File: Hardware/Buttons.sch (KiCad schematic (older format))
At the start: 12 parts, among them SW2 SW_Push, SW3 SW_Push, SW4 SW_Push

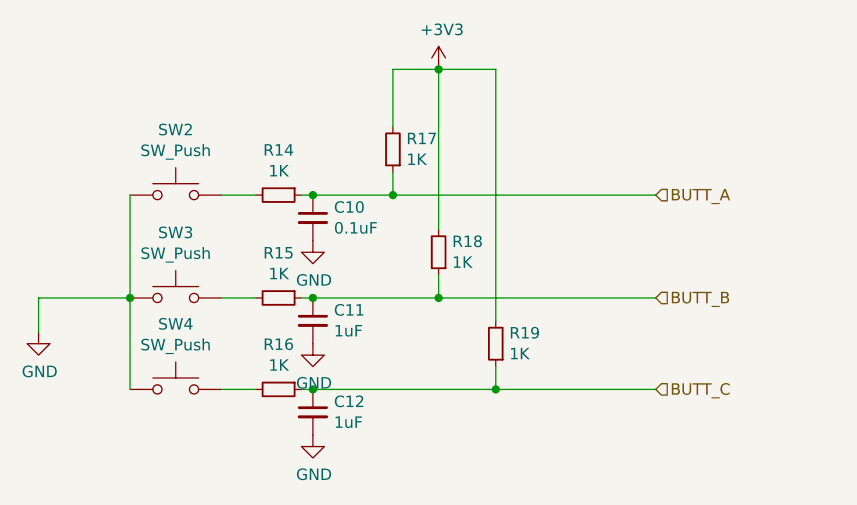
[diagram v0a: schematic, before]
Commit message: Added ADC instead of opamp. Added stiching
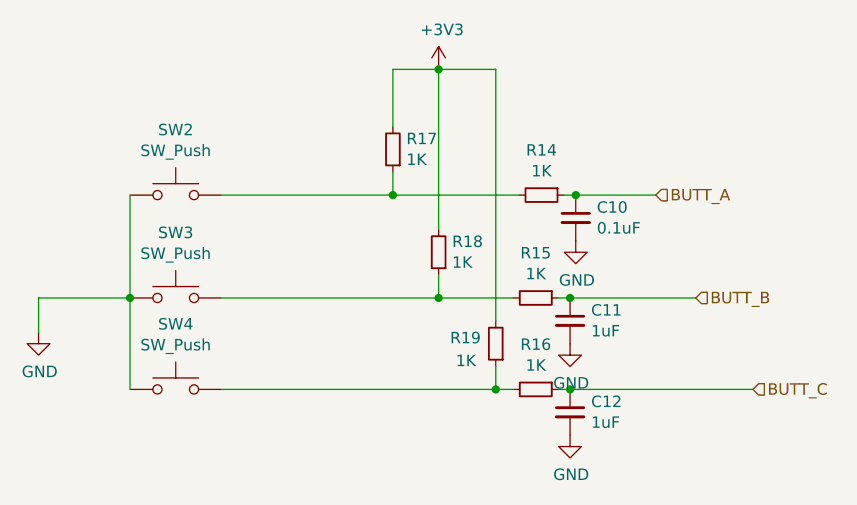
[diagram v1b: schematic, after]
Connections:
- net BUTT_A: no longer R17.1
- net BUTT_B: no longer R18.1
- net BUTT_C: no longer R19.1
- net at R14.2, SW2.2: now also R17.1
- net at R15.2, SW3.2: now also R18.1
- net at R16.2, SW4.2: now also R19.1
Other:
- moved on the sheet: C10, C11, C12, R14, R15, R16
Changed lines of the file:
@@
 L Device:R_Small R14
 U 1 1 5F81D440
-P 5450 2800
-F 0 "R14" V 5254 2800 50  0000 C CNN
-F 1 "1K" V 5345 2800 50  0000 C CNN
-F 2 "Resistor_SMD:R_0603_1608Metric_Pad1.05x0.95mm_HandSolder" H 5450 2800 50  0001 C CNN
-F 3 "~" H 5450 2800 50  0001 C CNN
-	1    5450 2800
+P 6600 2800
+F 0 "R14" V 6404 2800 50  0000 C CNN
+F 1 "1K" V 6495 2800 50  0000 C CNN
+F 2 "Resistor_SMD:R_0603_1608Metric_Pad1.05x0.95mm_HandSolder" H 6600 2800 50  0001 C CNN
+F 3 "~" H 6600 2800 50  0001 C CNN
+	1    6600 2800
 	0    1    1    0
 $EndComp
@@
 L Device:R_Small R15
 U 1 1 5F81DD10
-P 5450 3250
-F 0 "R15" V 5254 3250 50  0000 C CNN
-F 1 "1K" V 5345 3250 50  0000 C CNN
-F 2 "Resistor_SMD:R_0603_1608Metric_Pad1.05x0.95mm_HandSolder" H 5450 3250 50  0001 C CNN
-F 3 "~" H 5450 3250 50  0001 C CNN
-	1    5450 3250
+P 6575 3250
+F 0 "R15" V 6379 3250 50  0000 C CNN
+F 1 "1K" V 6470 3250 50  0000 C CNN
+F 2 "Resistor_SMD:R_0603_1608Metric_Pad1.05x0.95mm_HandSolder" H 6575 3250 50  0001 C CNN
+F 3 "~" H 6575 3250 50  0001 C CNN
+	1    6575 3250
 	0    1    1    0
 $EndComp
@@
 L Device:R_Small R16
 U 1 1 5F81E057
-P 5450 3650
-F 0 "R16" V 5254 3650 50  0000 C CNN
-F 1 "1K" V 5345 3650 50  0000 C CNN
-F 2 "Resistor_SMD:R_0603_1608Metric_Pad1.05x0.95mm_HandSolder" H 5450 3650 50  0001 C CNN
-F 3 "~" H 5450 3650 50  0001 C CNN
-	1    5450 3650
+P 6575 3650
+F 0 "R16" V 6379 3650 50  0000 C CNN
+F 1 "1K" V 6470 3650 50  0000 C CNN
+F 2 "Resistor_SMD:R_0603_1608Metric_Pad1.05x0.95mm_HandSolder" H 6575 3650 50  0001 C CNN
+F 3 "~" H 6575 3650 50  0001 C CNN
+	1    6575 3650
 	0    1    1    0
 $EndComp
@@
 L Device:C_Small C10
 U 1 1 5F81E4AB
-P 5600 2900
-F 0 "C10" H 5692 2946 50  0000 L CNN
-F 1 "0.1uF" H 5692 2855 50  0000 L CNN
-F 2 "Capacitor_SMD:C_0603_1608Metric_Pad1.05x0.95mm_HandSolder" H 5600 2900 50  0001 C CNN
-F 3 "~" H 5600 2900 50  0001 C CNN
-	1    5600 2900
+P 6750 2900
+F 0 "C10" H 6842 2946 50  0000 L CNN
+F 1 "0.1uF" H 6842 2855 50  0000 L CNN
+F 2 "Capacitor_SMD:C_0603_1608Metric_Pad1.05x0.95mm_HandSolder" H 6750 2900 50  0001 C CNN
+F 3 "~" H 6750 2900 50  0001 C CNN
+	1    6750 2900
 	1    0    0    -1
 $EndComp
@@
 L Device:C_Small C11
 U 1 1 5F81ED16
-P 5600 3350
-F 0 "C11" H 5692 3396 50  0000 L CNN
-F 1 "1uF" H 5692 3305 50  0000 L CNN
-F 2 "Capacitor_SMD:C_0603_1608Metric_Pad1.05x0.95mm_HandSolder" H 5600 3350 50  0001 C CNN
-F 3 "~" H 5600 3350 50  0001 C CNN
-	1    5600 3350
+P 6725 3350
+F 0 "C11" H 6817 3396 50  0000 L CNN
+F 1 "1uF" H 6817 3305 50  0000 L CNN
+F 2 "Capacitor_SMD:C_0603_1608Metric_Pad1.05x0.95mm_HandSolder" H 6725 3350 50  0001 C CNN
+F 3 "~" H 6725 3350 50  0001 C CNN
+	1    6725 3350
 	1    0    0    -1
 $EndComp
@@
 L Device:C_Small C12
 U 1 1 5F81F0E5
-P 5600 3750
-F 0 "C12" H 5692 3796 50  0000 L CNN
-F 1 "1uF" H 5692 3705 50  0000 L CNN
-F 2 "Capacitor_SMD:C_0603_1608Metric_Pad1.05x0.95mm_HandSolder" H 5600 3750 50  0001 C CNN
-F 3 "~" H 5600 3750 50  0001 C CNN
-	1    5600 3750
+P 6725 3750
+F 0 "C12" H 6817 3796 50  0000 L CNN
+F 1 "1uF" H 6817 3705 50  0000 L CNN
+F 2 "Capacitor_SMD:C_0603_1608Metric_Pad1.05x0.95mm_HandSolder" H 6725 3750 50  0001 C CNN
+F 3 "~" H 6725 3750 50  0001 C CNN
+	1    6725 3750
 	1    0    0    -1
 $EndComp
-Wire Wire Line
-	5200 2800 5350 2800
-Wire Wire Line
-	5200 3250 5350 3250
-Wire Wire Line
-	5200 3650 5350 3650
 $Comp
 L power:GND #PWR0129
 U 1 1 5F81F72F
-P 5600 3000
-F 0 "#PWR0129" H 5600 2750 50  0001 C CNN
-F 1 "GND" H 5605 2827 50  0000 C CNN
-F 2 "" H 5600 3000 50  0001 C CNN
-F 3 "" H 5600 3000 50  0001 C CNN
-	1    5600 3000
+P 6750 3000
+F 0 "#PWR0129" H 6750 2750 50  0001 C CNN
+F 1 "GND" H 6755 2827 50  0000 C CNN
+F 2 "" H 6750 3000 50  0001 C CNN
+F 3 "" H 6750 3000 50  0001 C CNN
+	1    6750 3000
 	1    0    0    -1
 $EndComp
@@
 L power:GND #PWR0130
 U 1 1 5F81FAA7
-P 5600 3450
-F 0 "#PWR0130" H 5600 3200 50  0001 C CNN
-F 1 "GND" H 5605 3277 50  0000 C CNN
-F 2 "" H 5600 3450 50  0001 C CNN
-F 3 "" H 5600 3450 50  0001 C CNN
-	1    5600 3450
+P 6725 3450
+F 0 "#PWR0130" H 6725 3200 50  0001 C CNN
+F 1 "GND" H 6730 3277 50  0000 C CNN
+F 2 "" H 6725 3450 50  0001 C CNN
+F 3 "" H 6725 3450 50  0001 C CNN
+	1    6725 3450
 	1    0    0    -1
 $EndComp
@@
 L power:GND #PWR0131
 U 1 1 5F81FF1B
-P 5600 3850
-F 0 "#PWR0131" H 5600 3600 50  0001 C CNN
-F 1 "GND" H 5605 3677 50  0000 C CNN
-F 2 "" H 5600 3850 50  0001 C CNN
-F 3 "" H 5600 3850 50  0001 C CNN
-	1    5600 3850
+P 6725 3850
+F 0 "#PWR0131" H 6725 3600 50  0001 C CNN
+F 1 "GND" H 6730 3677 50  0000 C CNN
+F 2 "" H 6725 3850 50  0001 C CNN
+F 3 "" H 6725 3850 50  0001 C CNN
+	1    6725 3850
 	1    0    0    -1
 $EndComp
 Wire Wire Line
-	5550 3650 5600 3650
+	6675 3650 6725 3650
 Wire Wire Line
-	5550 3250 5600 3250
+	6675 3250 6725 3250
 Wire Wire Line
-	5550 2800 5600 2800
+	6700 2800 6750 2800
 Wire Wire Line
-	5600 2800 5950 2800
-Connection ~ 5600 2800
-Connection ~ 5600 3250
-Connection ~ 5600 3650
+	6750 2800 7100 2800
+Connection ~ 6750 2800
+Connection ~ 6725 3250
+Connection ~ 6725 3650
 $Comp
 L Device:R_Small R17
@@
 U 1 1 5F82183D
 P 6400 3450
-F 0 "R19" H 6341 3404 50  0000 R CNN
-F 1 "1K" H 6341 3495 50  0000 R CNN
+F 0 "R19" H 6600 3425 50  0000 R CNN
+F 1 "1K" H 6575 3525 50  0000 R CNN
 F 2 "Resistor_SMD:R_0603_1608Metric_Pad1.05x0.95mm_HandSolder" H 6400 3450 50  0001 C CNN
 F 3 "~" H 6400 3450 50  0001 C CNN
@@
 	6150 3250 6150 3150
 Wire Wire Line
-	5600 3250 6150 3250
+	6725 3250 7275 3250
 Wire Wire Line
 	6150 2950 6150 2250
@@
 	6400 2250 6150 2250
 Wire Wire Line
-	5600 3650 6400 3650
-Wire Wire Line
 	6400 3350 6400 2250
 Wire Wire Line
-	5950 2800 7100 2800
+	6400 3650 6475 3650
+Text HLabel 7100 2800 2    50   Input ~ 0
+BUTT_A
+Text HLabel 7275 3250 2    50   Input ~ 0
+BUTT_B
+Text HLabel 7525 3650 2    50   Input ~ 0
+BUTT_C
+Wire Wire Line
+	5200 2800 5950 2800
 Connection ~ 5950 2800
 Wire Wire Line
-	6150 3250 7100 3250
+	5950 2800 6500 2800
+Wire Wire Line
+	5200 3250 6150 3250
 Connection ~ 6150 3250
 Wire Wire Line
-	6400 3650 7100 3650
+	6150 3250 6475 3250
+Wire Wire Line
+	6725 3650 7525 3650
+Wire Wire Line
+	5200 3650 6400 3650
 Connection ~ 6400 3650
-Text HLabel 7100 2800 2    50   Input ~ 0
-BUTT_A
-Text HLabel 7100 3250 2    50   Input ~ 0
-BUTT_B
-Text HLabel 7100 3650 2    50   Input ~ 0
-BUTT_C
 $EndSCHEMATC
